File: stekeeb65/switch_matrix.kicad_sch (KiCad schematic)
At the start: 134 parts

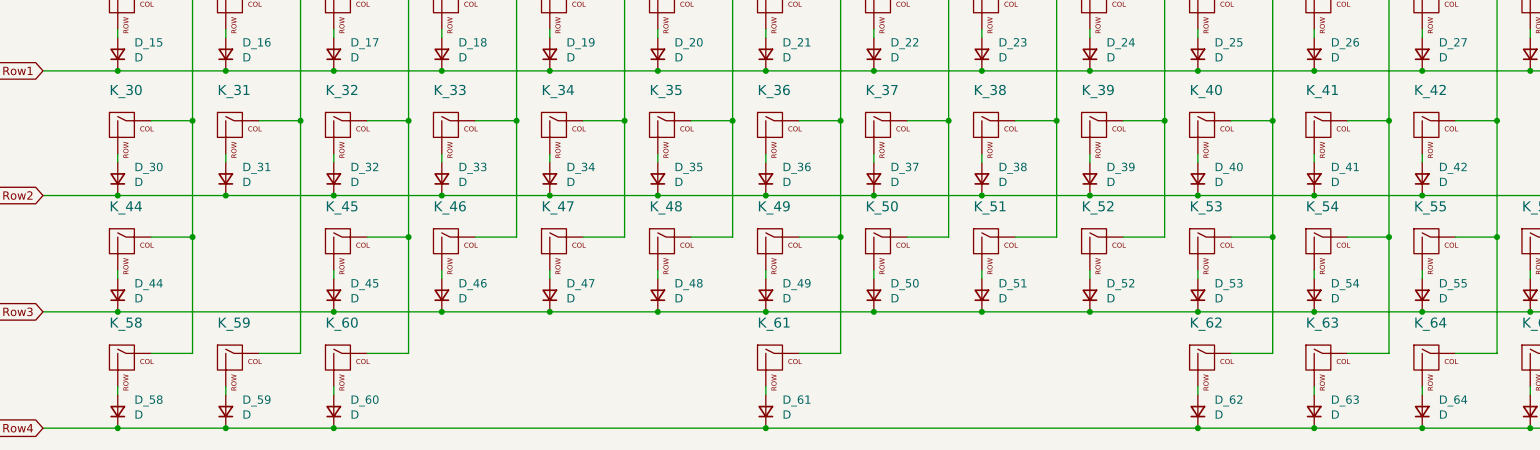
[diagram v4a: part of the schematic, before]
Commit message: Finish routing matrix
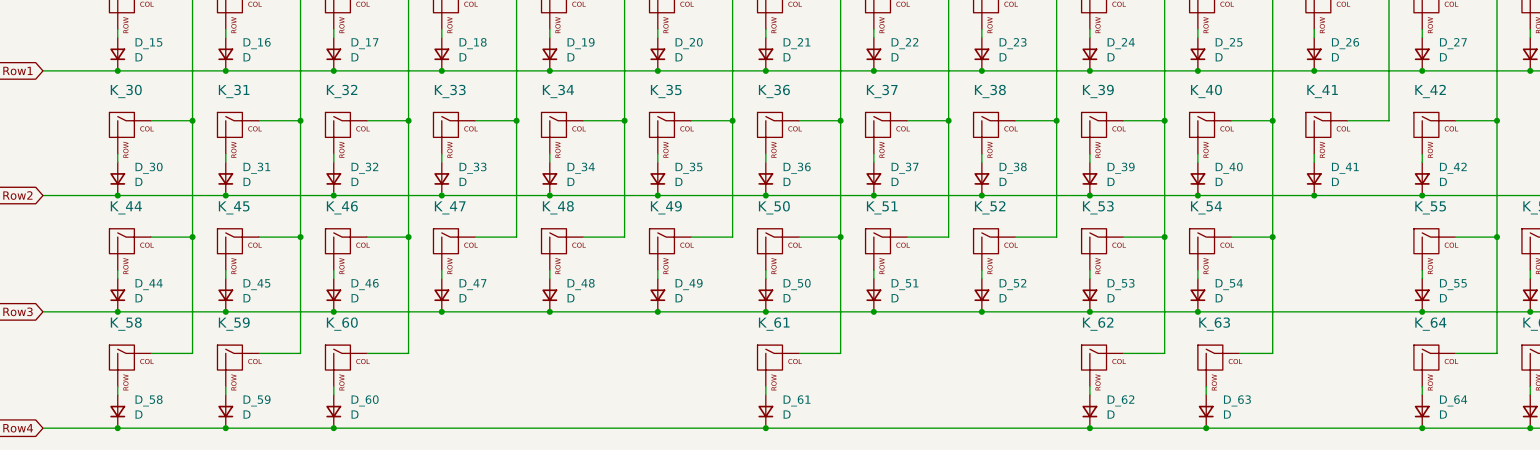
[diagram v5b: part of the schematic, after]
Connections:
- net Col1: now also K_45.1 (COL)
- net Col10: now also K_54.1 (COL), K_63.1 (COL); no longer K_53.1 (COL), K_62.1 (COL)
- net Col11: no longer K_54.1 (COL), K_63.1 (COL)
- net Col2: now also K_46.1 (COL); no longer K_45.1 (COL)
- net Col3: now also K_47.1 (COL); no longer K_46.1 (COL)
- net Col4: now also K_48.1 (COL); no longer K_47.1 (COL)
- net Col5: now also K_49.1 (COL); no longer K_48.1 (COL)
- net Col6: now also K_50.1 (COL); no longer K_49.1 (COL)
- net Col7: now also K_51.1 (COL); no longer K_50.1 (COL)
- net Col8: now also K_52.1 (COL); no longer K_51.1 (COL)
- net Col9: now also K_53.1 (COL), K_62.1 (COL); no longer K_52.1 (COL)
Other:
- moved on the sheet: D_45, D_46, D_47, D_48, D_49, D_50, D_51, D_52, D_53, D_54, D_62, D_63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

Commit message: Interim commit before potentially breaking stuff
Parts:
- added D_64: D, random-keyboard-parts:D_SOD-123-Pretty, symbol Device:D_Small
- added K_64: KEYSW, MX_Hotswap:MX-Hotswap-1U, symbol MX_Alps_Hybrid:MX-NoLED
- K_62, K_63: footprint MX_Hotswap:MX-Hotswap-1.25U -> MX_Hotswap:MX-Hotswap-1U
- renumbered D_64 to D_65, D_65 to D_66, D_66 to D_67, K_64 to K_65, K_65 to K_66, K_66 to K_67
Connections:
- net Col11: now also K_64.1 (COL)
- net Row4: now also D_64.1 (K)
- new net: D_64.2 (A), K_64.2 (ROW)
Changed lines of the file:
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@@
   (junction (at 166.37 88.9) (diameter 0) (color 0 0 0 0)
   )
+  (junction (at 228.6 96.52) (diameter 0) (color 0 0 0 0)
+  )
   (junction (at 276.86 96.52) (diameter 0) (color 0 0 0 0)
   )
@@
   (junction (at 144.78 58.42) (diameter 0) (color 0 0 0 0)
   )
+  (junction (at 217.17 143.51) (diameter 0) (color 0 0 0 0)
+  )
   (junction (at 133.35 69.85) (diameter 0) (color 0 0 0 0)
   )
@@
     (stroke (width 0) (type default) (color 0 0 0 0))
   )
+  (wire (pts (xy 217.17 137.16) (xy 217.17 138.43))
+    (stroke (width 0) (type default) (color 0 0 0 0))
+  )
   (wire (pts (xy 199.39 119.38) (xy 199.39 120.65))
     (stroke (width 0) (type default) (color 0 0 0 0))
@@
     (stroke (width 0) (type default) (color 0 0 0 0))
   )
+  (wire (pts (xy 228.6 132.08) (xy 228.6 96.52))
+    (stroke (width 0) (type default) (color 0 0 0 0))
+  )
   (wire (pts (xy 67.31 137.16) (xy 67.31 138.43))
     (stroke (width 0) (type default) (color 0 0 0 0))
@@
     (stroke (width 0) (type default) (color 0 0 0 0))
   )
-  (wire (pts (xy 200.66 143.51) (xy 233.68 143.51))
+  (wire (pts (xy 200.66 143.51) (xy 217.17 143.51))
     (stroke (width 0) (type default) (color 0 0 0 0))
   )
@@
     (stroke (width 0) (type default) (color 0 0 0 0))
   )
+  (wire (pts (xy 222.25 132.08) (xy 228.6 132.08))
+    (stroke (width 0) (type default) (color 0 0 0 0))
+  )
   (wire (pts (xy 233.68 69.85) (xy 250.19 69.85))
     (stroke (width 0) (type default) (color 0 0 0 0))
@@
     (stroke (width 0) (type default) (color 0 0 0 0))
   )
+  (wire (pts (xy 217.17 143.51) (xy 233.68 143.51))
+    (stroke (width 0) (type default) (color 0 0 0 0))
+  )
   (wire (pts (xy 50.8 63.5) (xy 50.8 64.77))
     (stroke (width 0) (type default) (color 0 0 0 0))
@@
   (symbol (lib_id "MX_Alps_Hybrid:MX-NoLED") (at 266.7 133.35 0) (unit 1)
     (in_bom yes) (on_board yes)
-    (property "Reference" "K_66" (id 0) (at 266.7 127.4318 0)
+    (property "Reference" "K_67" (id 0) (at 266.7 127.4318 0)
       (effects (font (size 1.524 1.524)))
     )
@@
   (symbol (lib_id "Device:D_Small") (at 233.68 140.97 90) (unit 1)
     (in_bom yes) (on_board yes)
-    (property "Reference" "D_64" (id 0) (at 236.22 139.192 90)
+    (property "Reference" "D_65" (id 0) (at 236.22 139.192 90)
       (effects (font (size 1.27 1.27)) (justify right))
     )
@@
   (symbol (lib_id "MX_Alps_Hybrid:MX-NoLED") (at 251.46 133.35 0) (unit 1)
     (in_bom yes) (on_board yes)
-    (property "Reference" "K_65" (id 0) (at 251.46 127.4318 0)
+    (property "Reference" "K_66" (id 0) (at 251.46 127.4318 0)
       (effects (font (size 1.524 1.524)))
     )
@@
   (symbol (lib_id "Device:D_Small") (at 250.19 140.97 90) (unit 1)
     (in_bom yes) (on_board yes)
-    (property "Reference" "D_65" (id 0) (at 252.73 139.192 90)
+    (property "Reference" "D_66" (id 0) (at 252.73 139.192 90)
       (effects (font (size 1.27 1.27)) (justify right))
     )
@@
     (pin "2")
   )
+  (symbol (lib_id "MX_Alps_Hybrid:MX-NoLED") (at 218.44 133.35 0) (unit 1)
+    (in_bom yes) (on_board yes)
+    (property "Reference" "K_64" (id 0) (at 218.44 127.4318 0)
+      (effects (font (size 1.524 1.524)))
+    )
+    (property "Value" "KEYSW" (id 1) (at 218.44 135.89 0)
+      (effects (font (size 1.524 1.524)) hide)
+    )
+    (property "Footprint" "MX_Hotswap:MX-Hotswap-1U" (id 2) (at 218.44 133.35 0)
+      (effects (font (size 1.524 1.524)) hide)
+    )
+    (property "Datasheet" "" (id 3) (at 218.44 133.35 0)
+      (effects (font (size 1.524 1.524)))
+    )
+    (pin "1")
+    (pin "2")
+  )
   (symbol (lib_id "Device:D_Small") (at 116.84 123.19 90) (unit 1)
     (in_bom yes) (on_board yes)
@@
   (symbol (lib_id "MX_Alps_Hybrid:MX-NoLED") (at 234.95 133.35 0) (unit 1)
     (in_bom yes) (on_board yes)
-    (property "Reference" "K_64" (id 0) (at 234.95 127.4318 0)
+    (property "Reference" "K_65" (id 0) (at 234.95 127.4318 0)
       (effects (font (size 1.524 1.524)))
     )
@@
     (pin "2")
   )
+  (symbol (lib_id "Device:D_Small") (at 217.17 140.97 90) (unit 1)
+    (in_bom yes) (on_board yes)
+    (property "Reference" "D_64" (id 0) (at 219.71 139.192 90)
+      (effects (font (size 1.27 1.27)) (justify right))
+    )
+    (property "Value" "D" (id 1) (at 219.71 141.478 90)
+      (effects (font (size 1.27 1.27)) (justify right))
+    )
+    (property "Footprint" "random-keyboard-parts:D_SOD-123-Pretty" (id 2) (at 218.44 148.59 0)
+      (effects (font (size 1.27 1.27)) hide)
+    )
+    (property "Datasheet" "~" (id 3) (at 218.44 148.59 0)
+      (effects (font (size 1.27 1.27)) hide)
+    )
+    (pin "1")
+    (pin "2")
+  )
   (symbol (lib_id "MX_Alps_Hybrid:MX-NoLED") (at 200.66 97.79 0) (unit 1)
     (in_bom yes) (on_board yes)
@@
       (effects (font (size 1.524 1.524)) hide)
     )
-    (property "Footprint" "MX_Hotswap:MX-Hotswap-1.25U" (id 2) (at 201.93 133.35 0)
+    (property "Footprint" "MX_Hotswap:MX-Hotswap-1U" (id 2) (at 201.93 133.35 0)
       (effects (font (size 1.524 1.524)) hide)
     )
@@
   (symbol (lib_id "Device:D_Small") (at 265.43 140.97 90) (unit 1)
     (in_bom yes) (on_board yes)
-    (property "Reference" "D_66" (id 0) (at 267.97 139.192 90)
+    (property "Reference" "D_67" (id 0) (at 267.97 139.192 90)
       (effects (font (size 1.27 1.27)) (justify right))
     )
@@
       (effects (font (size 1.524 1.524)) hide)
     )
-    (property "Footprint" "MX_Hotswap:MX-Hotswap-1.25U" (id 2) (at 184.15 133.35 0)
+    (property "Footprint" "MX_Hotswap:MX-Hotswap-1U" (id 2) (at 184.15 133.35 0)
       (effects (font (size 1.524 1.524)) hide)
     )
